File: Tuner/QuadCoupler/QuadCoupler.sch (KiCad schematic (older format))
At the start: 89 parts, among them J1 Conn_01x02, J10 Conn_01x02, J2 Conn_Coaxial, J21 Conn_01x01, J22 Conn_01x01, J23 Conn_01x01, J24 Conn_01x01, J3 Conn_Coaxial, J4 Conn_Coaxial, J5 Conn_Coaxial, J6 Conn_Coaxial, J7 Conn_01x02, J8 Conn_01x02, J9 Conn_01x02

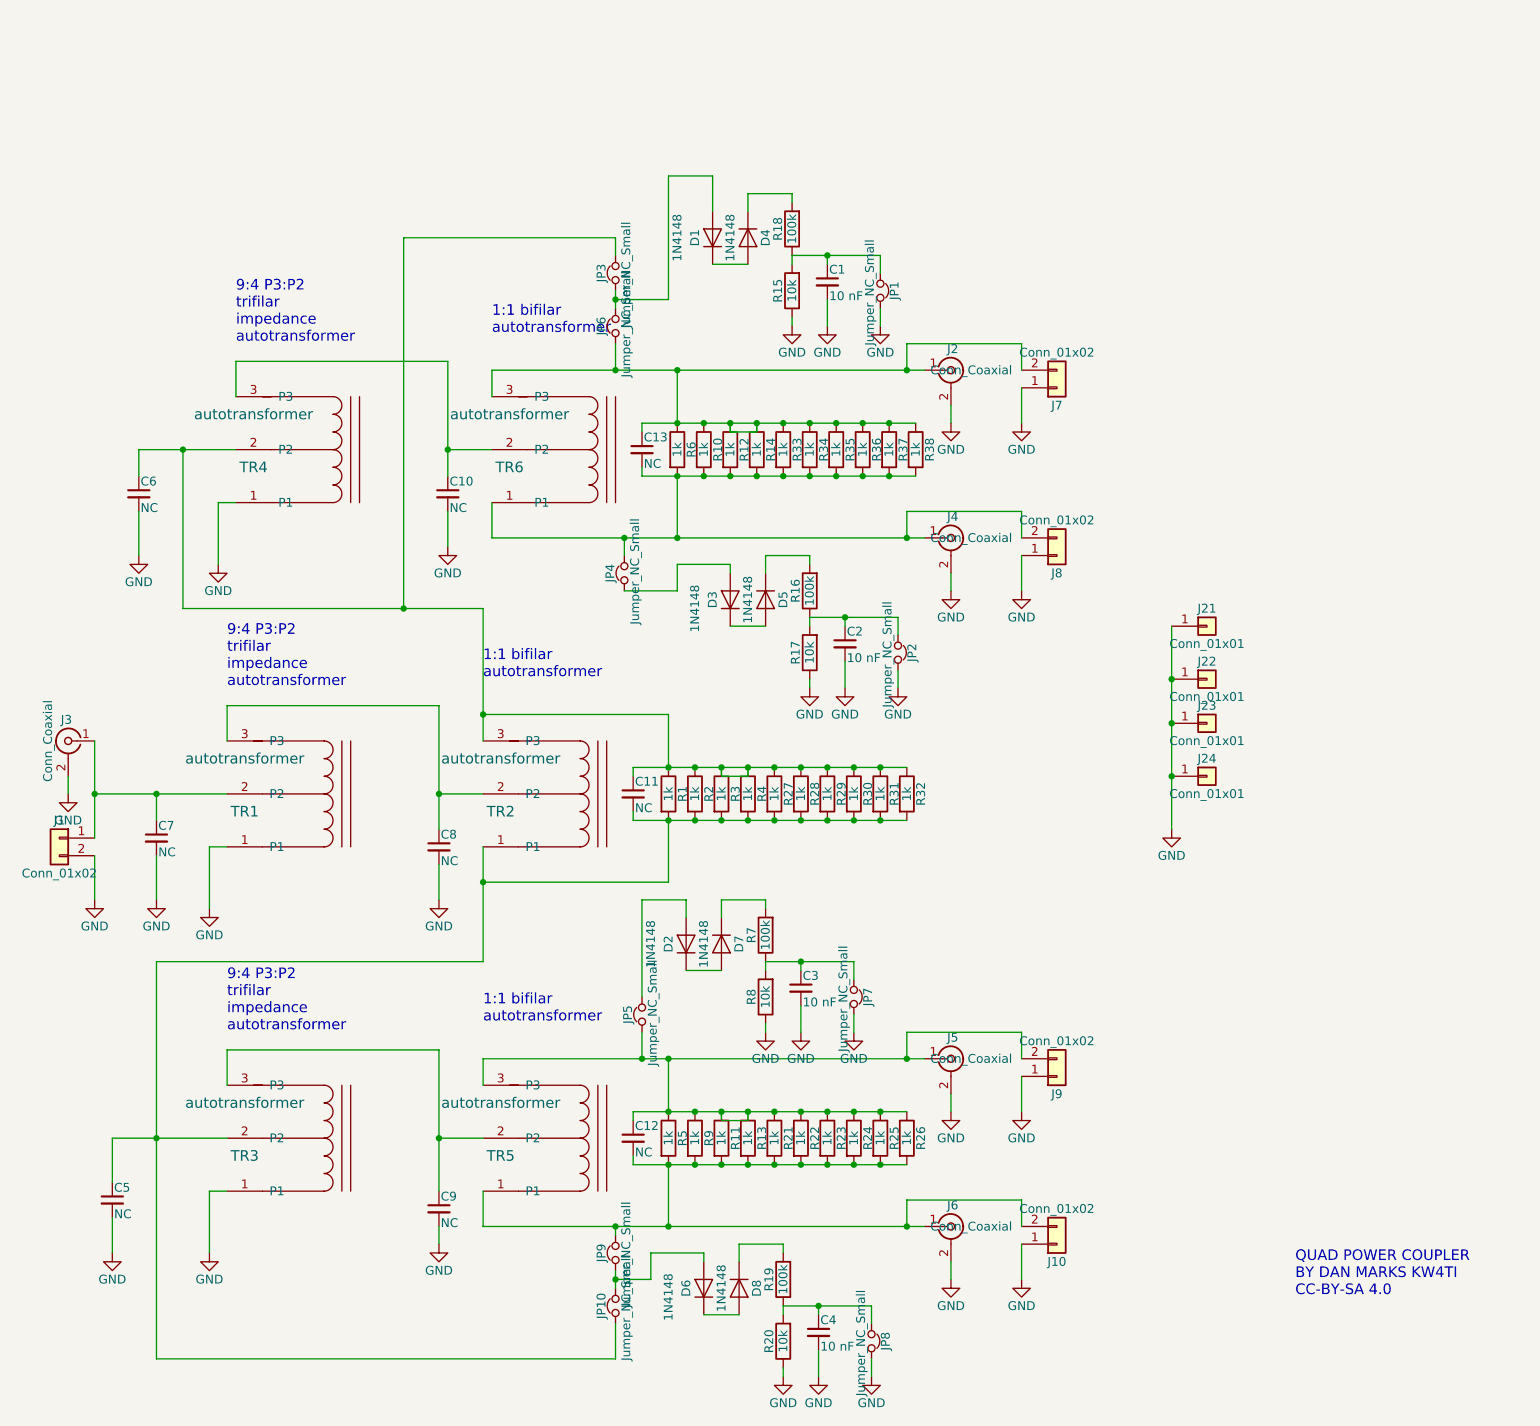
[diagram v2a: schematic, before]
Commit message: Added BNC and screw terminal combo pads
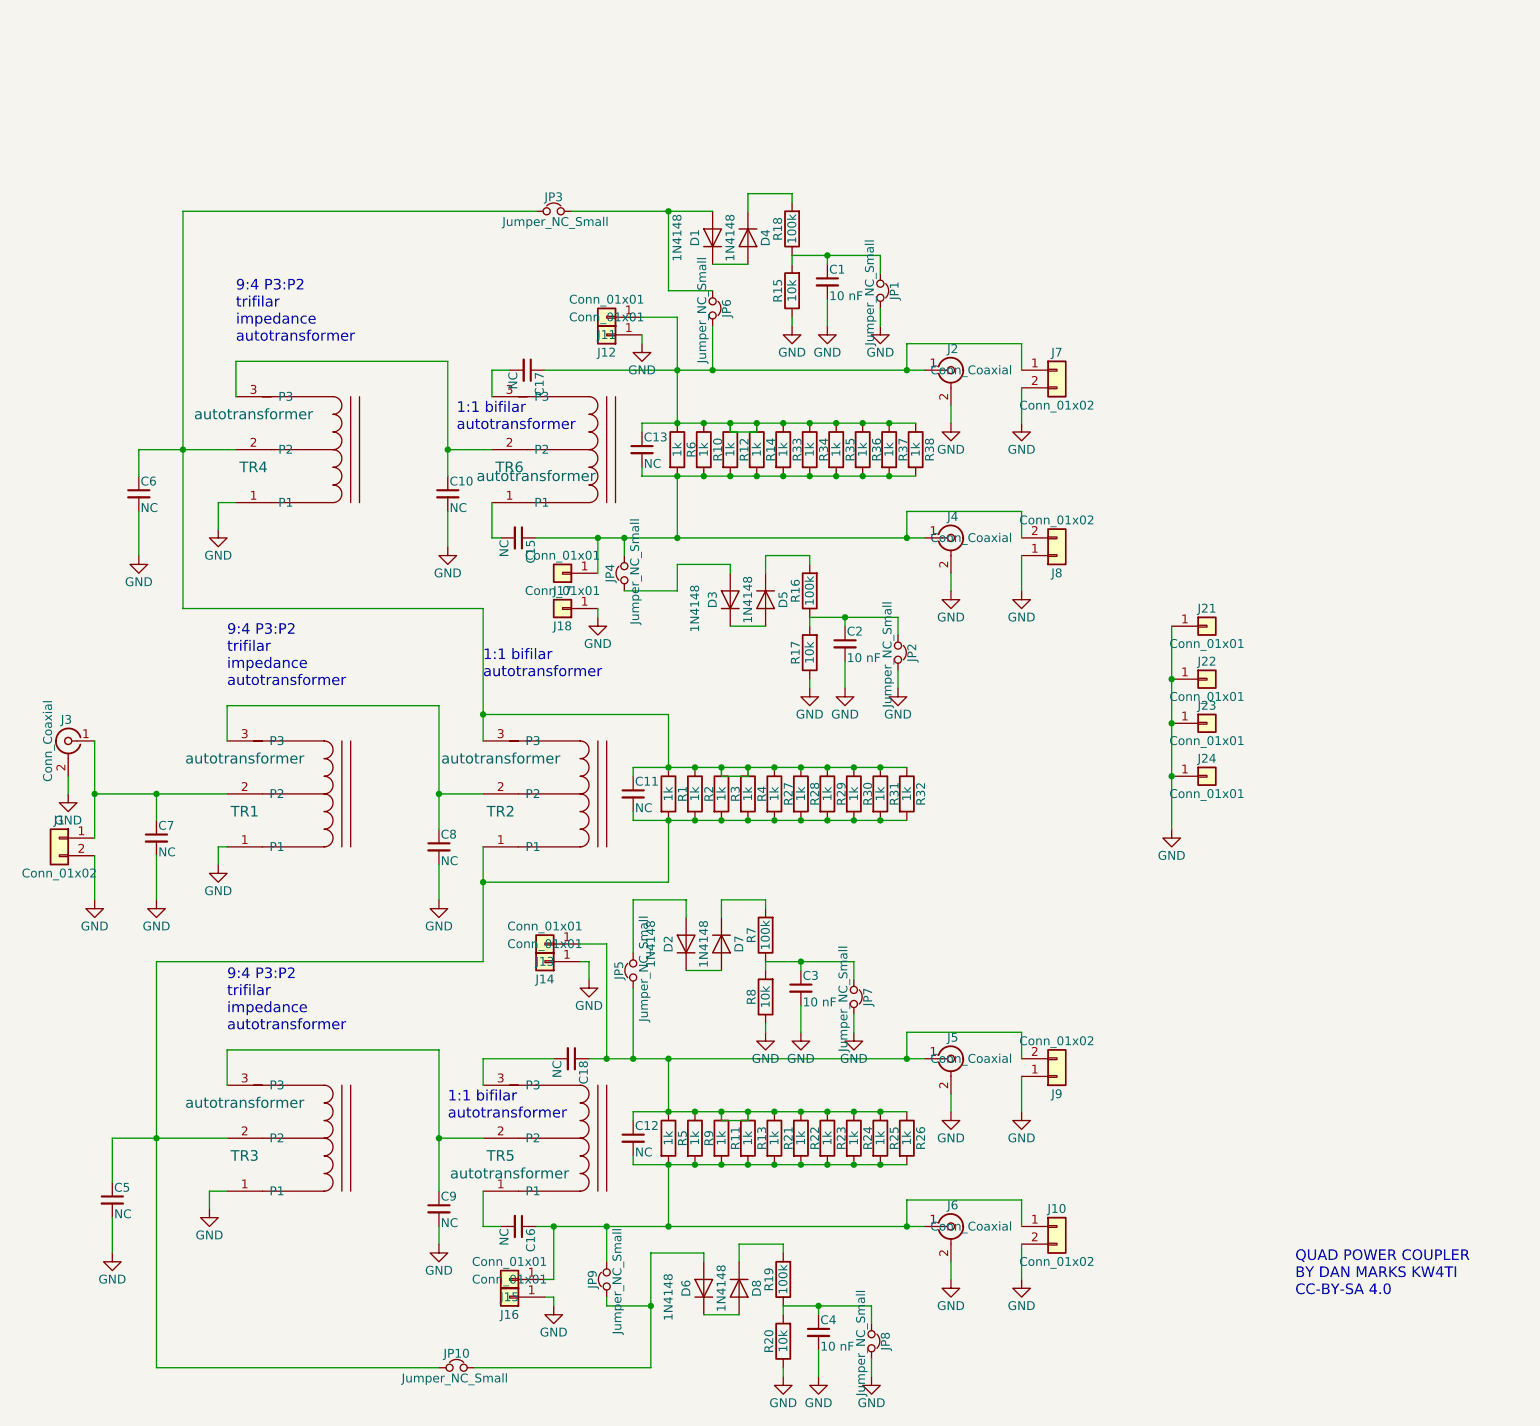
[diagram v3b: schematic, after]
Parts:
- added C15, C16, C17, C18: NC, Capacitors_THT:C_Disc_D5.0mm_W2.5mm_P5.00mm, symbol C_Small
- added J11, J12, J13, J14, J15, J16, J17, J18: Conn_01x01, Connectors:1pin, symbol Conn_01x01
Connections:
- net GND: now also J10.2 (Pin_2), J7.2 (Pin_2), J12.1 (Pin_1), J14.1 (Pin_1), J16.1 (Pin_1), J18.1 (Pin_1); no longer J10.1 (Pin_1), J7.1 (Pin_1)
- net at C13.2, J4.1 (In), J8.2 (Pin_2)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: now also C15.1, J17.1 (Pin_1); no longer TR6.1 (P1)
- net at C13.1, J2.1 (In), R10.1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: now also J7.1 (Pin_1), JP6.2, C17.1, J11.1 (Pin_1); no longer J7.2 (Pin_2), JP6.1, TR6.3 (P3)
- net at C12.2, J6.1 (In), JP9.1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: now also J10.1 (Pin_1), C16.1, J15.1 (Pin_1); no longer J10.2 (Pin_2), TR5.1 (P1)
- net at C12.1, J5.1 (In), J9.2 (Pin_2)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: now also C18.1, J13.1 (Pin_1); no longer TR5.3 (P3)
- net at D1.2 (A), JP3.2: now also JP6.1; no longer JP6.2
- new net: C15.2, TR6.1 (P1)
- new net: C17.2, TR6.3 (P3)
- new net: C16.2, TR5.1 (P1)
- new net: C18.2, TR5.3 (P3)
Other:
- moved on the sheet: JP10, JP3, JP5, JP6, JP9

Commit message: Changed over yet more to BNC
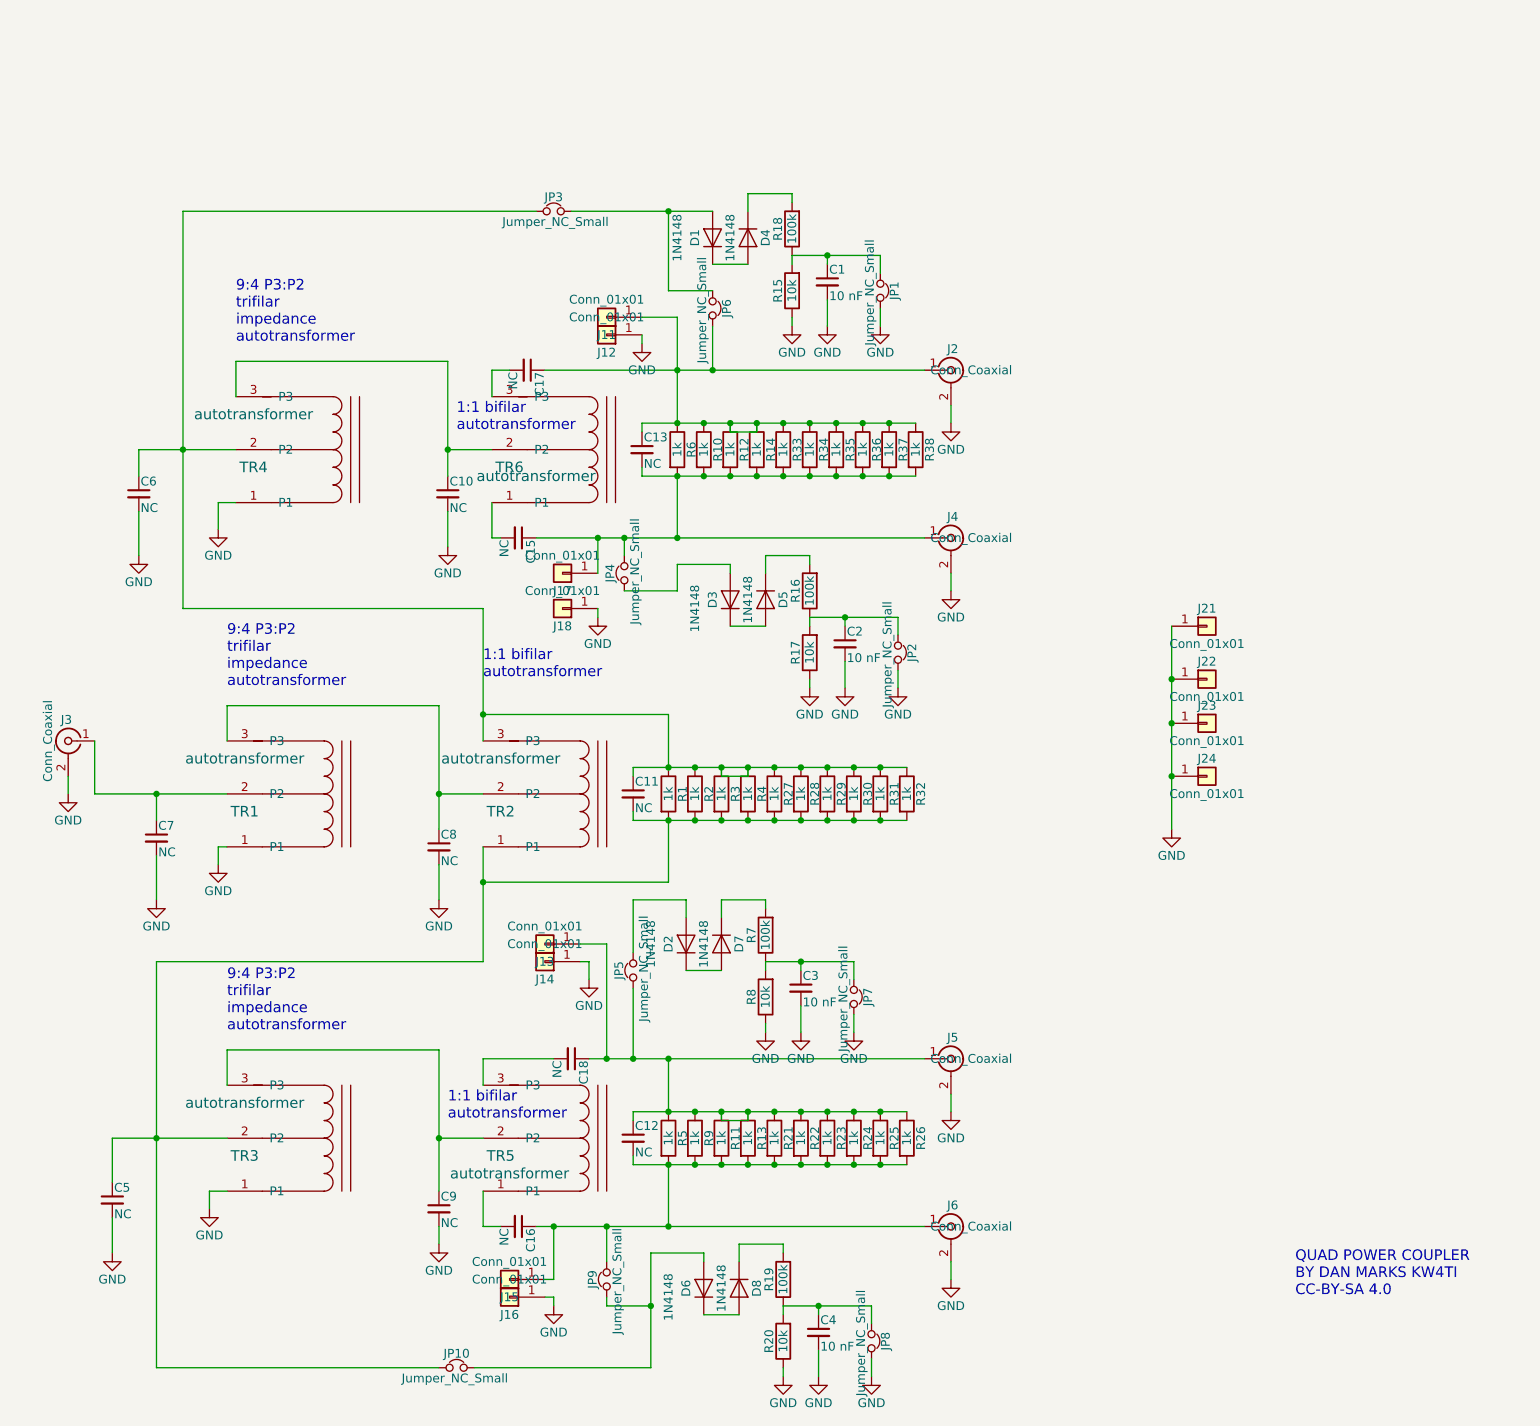
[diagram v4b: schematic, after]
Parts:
- removed J1, J10, J7, J8, J9: Conn_01x02, Connectors_Terminal_Blocks:TerminalBlock_bornier-2_P5.08mm, symbol Conn_01x02
- J2, J3, J4, J5, J6: footprint QuadCoupler:bnc_90_1-1337543-0 -> QuadCoupler:bnc_90_1-1337543-0_pad_combo

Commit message: TandenMatch now has DC-RF bias tee
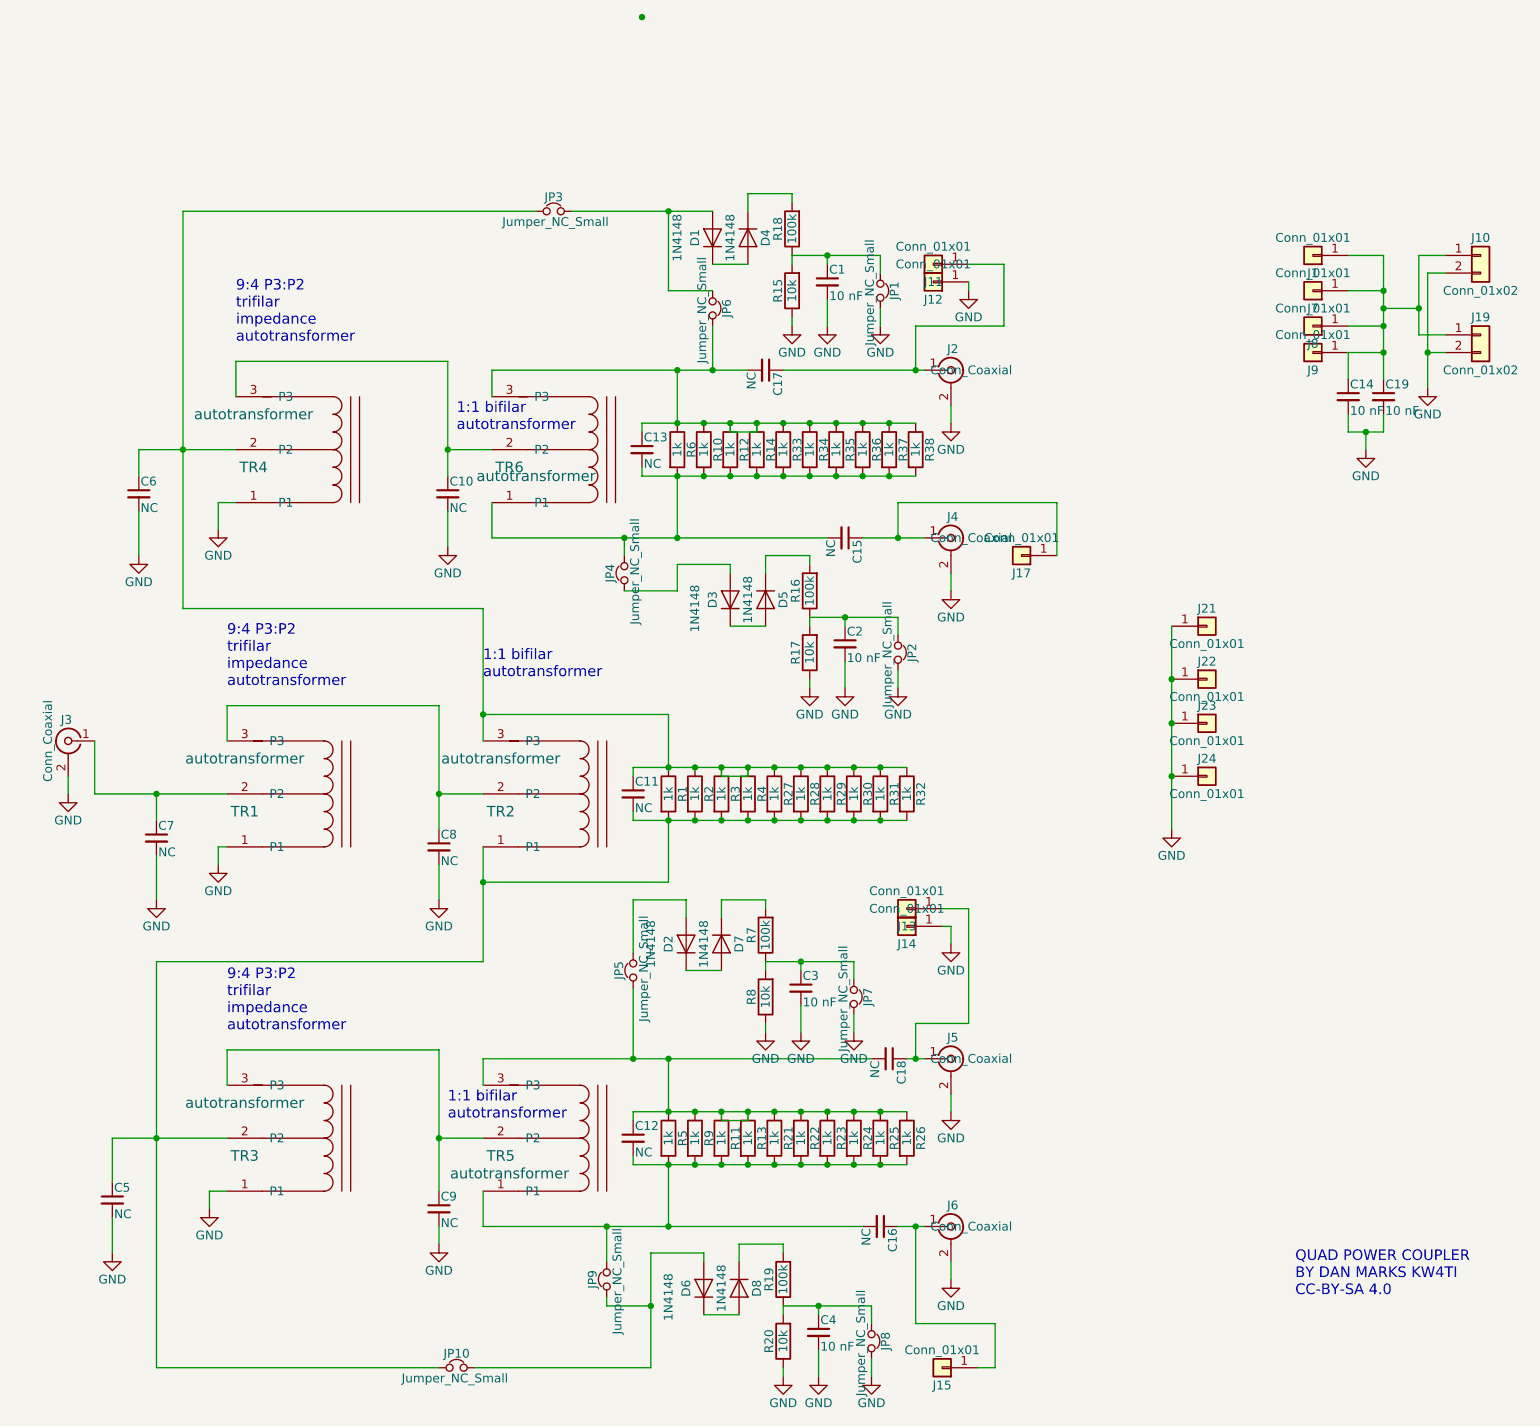
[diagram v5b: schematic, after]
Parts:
- removed J16, J18: Conn_01x01, Connectors:1pin, symbol Conn_01x01
- added C14, C19: 10 nF, Capacitors_THT:C_Disc_D5.0mm_W2.5mm_P5.00mm, symbol C_Small
- added J1, J7, J8, J9: Conn_01x01, Connectors:1pin, symbol Conn_01x01
- added J10, J19: Conn_01x02, Connectors_Terminal_Blocks:TerminalBlock_bornier-2_P5.08mm, symbol Conn_01x02
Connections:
- net GND: now also C14.2, C19.2, J10.2 (Pin_2), J19.2 (Pin_2)
- net at C15.2, TR6.1 (P1): now also C13.2, JP4.2, R10.2, R12.2, R14.2, R33.2, R34.2, R35.2, R36.2, R37.2, R38.2, R6.2
- net at C17.2, TR6.3 (P3): now also C13.1, JP6.2, R10.1, R12.1, R14.1, R33.1, R34.1, R35.1, R36.1, R37.1, R38.1, R6.1
- net at C16.2, TR5.1 (P1): now also C12.2, JP9.1, R11.2, R13.2, R21.2, R22.2, R23.2, R24.2, R25.2, R26.2, R5.2, R9.2
- net at C18.2, TR5.3 (P3): now also C12.1, JP5.1, R11.1, R13.1, R21.1, R22.1, R23.1, R24.1, R25.1, R26.1, R5.1, R9.1
- new net: C17.1, J11.1 (Pin_1), J2.1 (In)
- new net: C15.1, J17.1 (Pin_1), J4.1 (In)
- new net: C18.1, J13.1 (Pin_1), J5.1 (In)
- new net: C16.1, J15.1 (Pin_1), J6.1 (In)
- new net: C14.1, C19.1, J1.1 (Pin_1), J10.1 (Pin_1), J19.1 (Pin_1), J7.1 (Pin_1), J8.1 (Pin_1), J9.1 (Pin_1)
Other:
- moved on the sheet: C15, C16, C17, C18, J11, J12, J13, J14, J15, J17
